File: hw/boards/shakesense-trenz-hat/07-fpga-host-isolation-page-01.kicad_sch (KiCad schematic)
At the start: 12 parts, among them Q1 2N7002, U51 TXU0202DCUR, U52 TLV803EA30DBZR

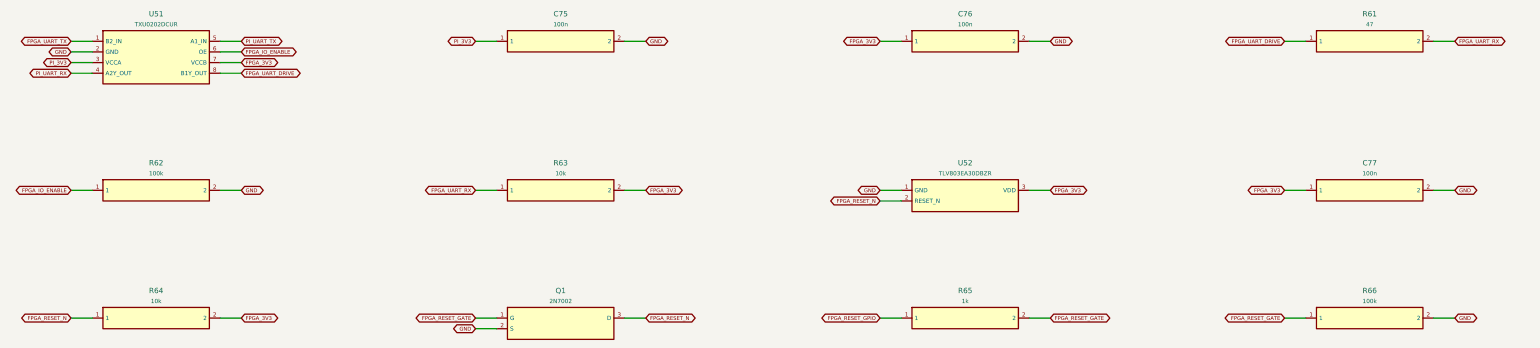
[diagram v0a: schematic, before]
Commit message: Expose Trenz GPIOs on the Pi-outline HDI sensor HAT
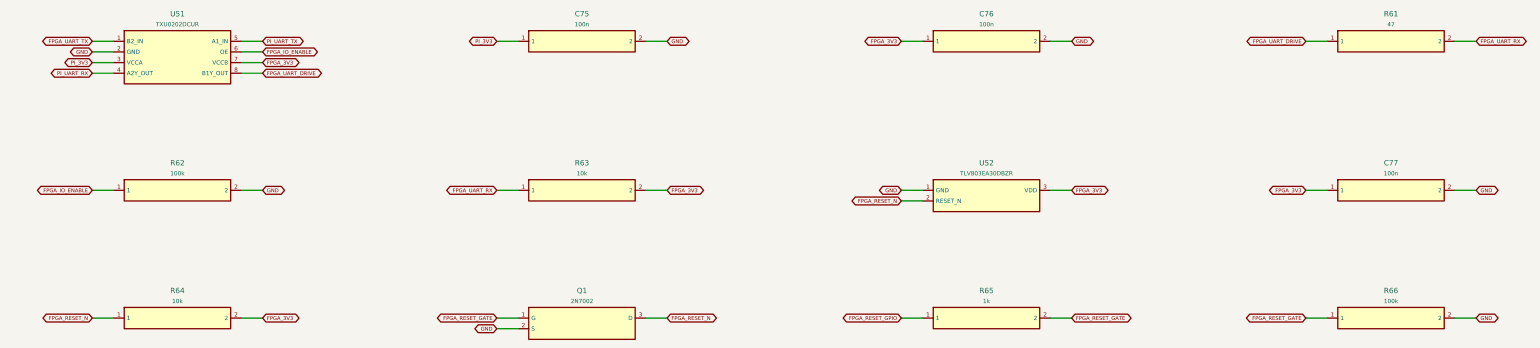
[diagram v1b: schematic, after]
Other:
- title: shakesense-trenz-hat / 07-fpga-host-isolation-page-01 -> ShakeSense T1 / 07-fpga-host-isolation-page-01
- moved on the sheet: C75, C76, C77, Q1, R61, R62, R63, R64, R65, R66, U51, U52
